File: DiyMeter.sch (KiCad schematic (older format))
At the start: 87 parts

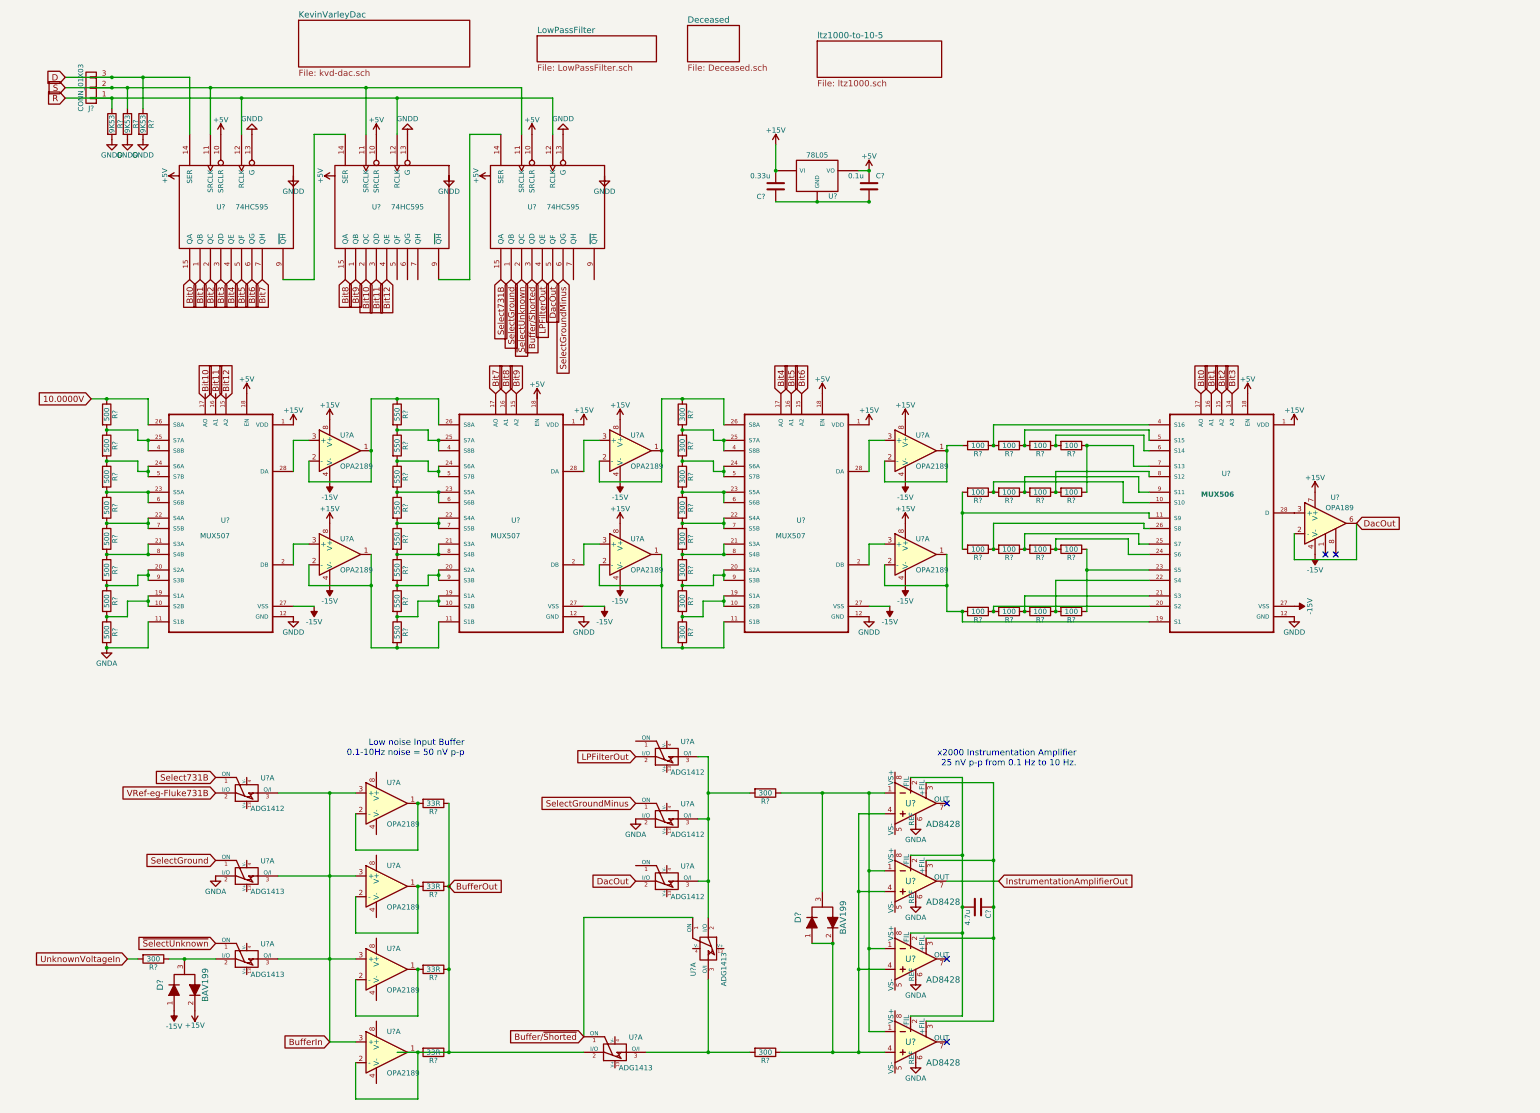
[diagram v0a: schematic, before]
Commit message: Add files via upload
Updated opamps to ada4522 because they have lower bias current.
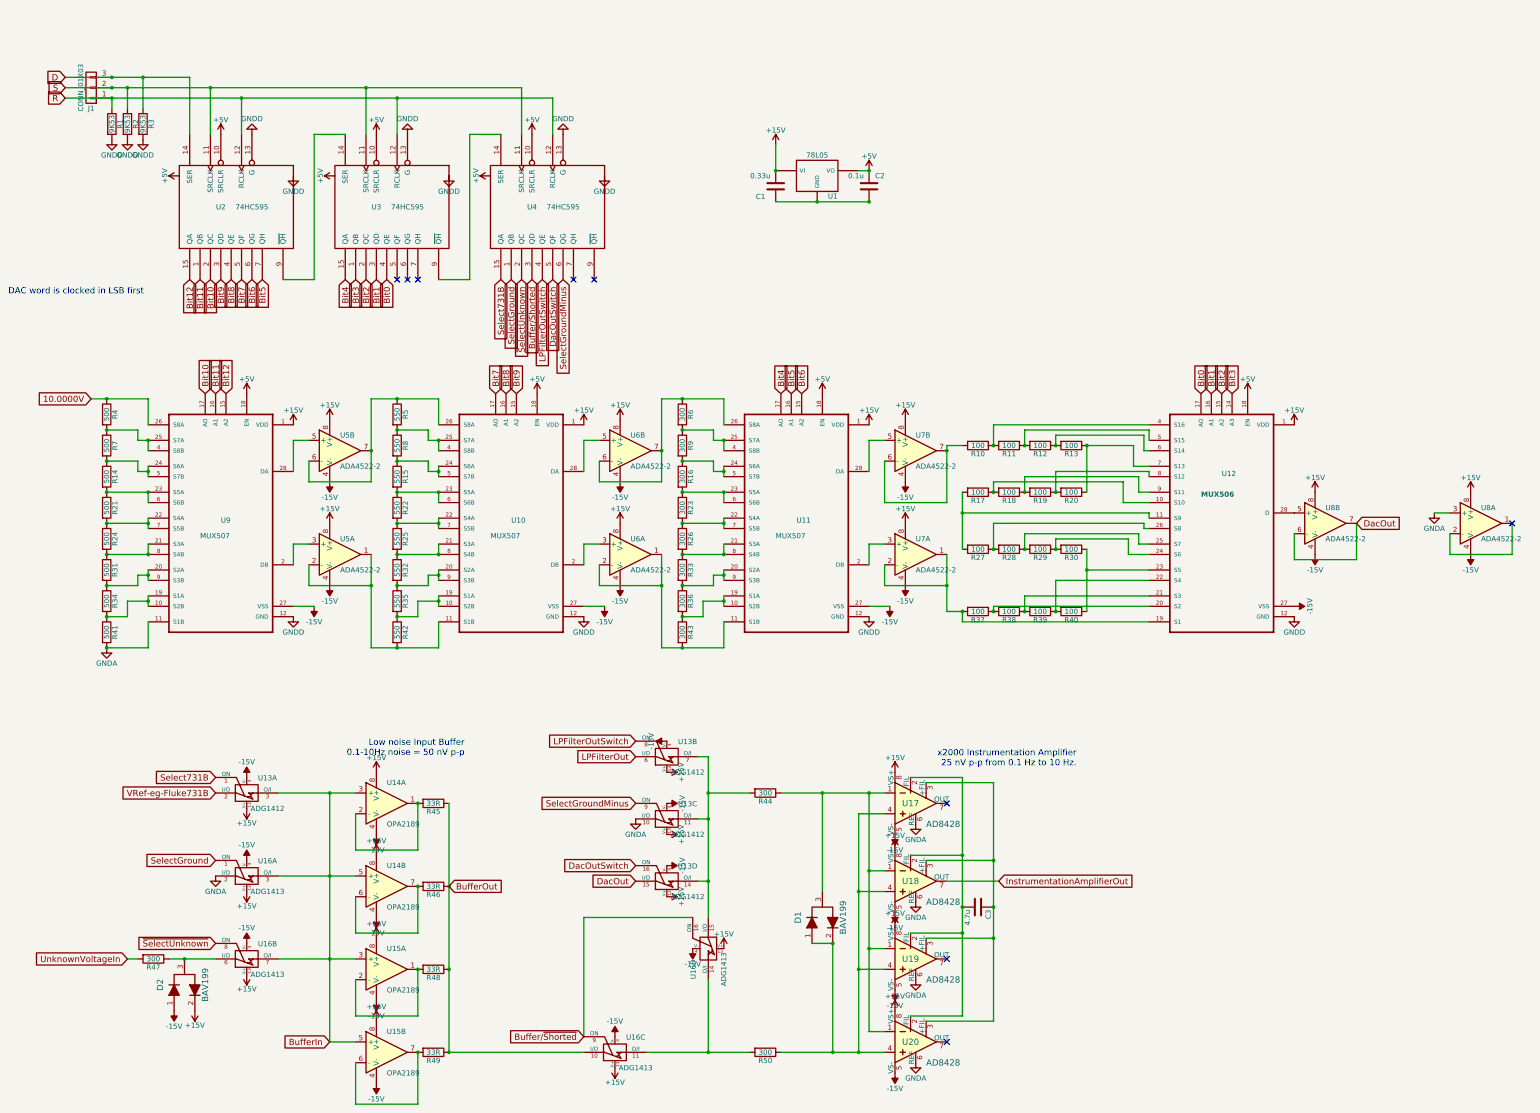
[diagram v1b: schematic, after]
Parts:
- removed U?: OPA189, symbol OP07
- added U8: ADA4522-2, symbol OP275
- U5, U6, U7: renamed from U?; value OPA2189 -> ADA4522-2
- gave numbers to parts that had none: 72
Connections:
- net +15V: now also U13.13 (V+), U13.13 (V+), U13.13 (V+), U13.13 (V+), U14.8 (V+), U14.8 (V+), U15.8 (V+), U15.8 (V+), U16.13 (V+), U16.13 (V+), U16.13 (V+), U16.13 (V+), U17.8 (VS+), U18.8 (VS+), U19.8 (VS+), U20.8 (VS+), U8.8 (V+), U8.8 (V+)
- net +5V: now also U10.18 (EN)
- net -15V: now also U13.4 (V-), U13.4 (V-), U13.4 (V-), U13.4 (V-), U14.4 (V-), U14.4 (V-), U15.4 (V-), U15.4 (V-), U16.4 (V-), U16.4 (V-), U16.4 (V-), U16.4 (V-), U17.5 (VS-), U18.5 (VS-), U19.5 (VS-), U20.5 (VS-), U8.4 (V-), U8.4 (V-)
- net Bit0: now also U3.4 (QE); no longer U2.15 (QA)
- net Bit1: now also U3.3 (QD); no longer U2.1 (QB)
- net Bit10: now also U2.2 (QC), U9.17 (AO); no longer U3.2 (QC)
- net Bit11: now also U2.1 (QB), U9.16 (A1); no longer U3.3 (QD)
- net Bit12: now also U2.15 (QA), U9.15 (A2); no longer U3.4 (QE)
- net Bit2: now also U3.2 (QC); no longer U2.2 (QC)
- net Bit3: now also U3.1 (QB); no longer U2.3 (QD)
- net Bit4: now also U3.15 (QA); no longer U2.4 (QE)
- net Bit5: now also U2.7 (QH); no longer U2.5 (QF)
- net Bit7: now also U2.5 (QF); no longer U2.7 (QH)
- net Bit8: now also U2.4 (QE); no longer U3.15 (QA)
- net Bit9: now also U2.3 (QD); no longer U3.1 (QB)
- net Buffer/~Shorted: now also U16.16 (ON), U16.9 (ON); no longer U16.1 (ON), U16.1 (ON)
- net BufferIn: now also U14.5 (+), U15.5 (+), U16.7 (O/I); no longer U14.3 (+), U15.3 (+), U16.3 (O/I)
- net BufferOut: now also U16.10 (I/O); no longer R49.2, U15.1, U15.2 (-), U16.2 (I/O)
- net DacOut: now also U13.15 (I/O), U8.6 (-), U8.7; no longer U13.2 (I/O), U4.5 (QF)
- net GNDA: now also U13.10 (I/O), U8.3 (+); no longer U13.2 (I/O)
- net LPFilterOut: now also U13.6 (I/O); no longer U13.2 (I/O), U4.4 (QE)
- net SelectGroundMinus: now also U13.9 (ON); no longer U13.1 (ON)
- net ~SelectUnknown: now also U16.8 (ON); no longer U16.1 (ON)
- net at U9.2 (DB): now also U5.3 (+); no longer U5.3 (+)
- net at U9.28 (DA): now also U5.5 (+); no longer U5.3 (+)
- net at R42.2, U10.11 (S1B): now also U5.1, U5.2 (-); no longer U5.1, U5.2 (-)
- net at R5.1, U10.26 (S8A): now also U5.6 (-), U5.7; no longer U5.1, U5.2 (-)
- net at U10.2 (DB): now also U6.3 (+); no longer U6.3 (+)
- net at U10.28 (DA): now also U6.5 (+); no longer U6.3 (+)
- net at R43.2, U11.11 (S1B): now also U6.1, U6.2 (-); no longer U6.1, U6.2 (-)
- net at R6.1, U11.26 (S8A): now also U6.6 (-), U6.7; no longer U6.1, U6.2 (-)
- net at U11.2 (DB): now also U7.3 (+); no longer U7.3 (+)
- net at U11.28 (DA): now also U7.5 (+); no longer U7.3 (+)
- net at R37.2, U12.19 (S1): now also U7.1, U7.2 (-); no longer U7.1, U7.2 (-)
- net at U12.28 (D): now also U8.5 (+)
- net at D2.3, R47.1: now also U16.6 (I/O); no longer U16.2 (I/O)
- new net: R10.2, U7.6 (-), U7.7
- new net: R44.2, U13.11 (O/I), U13.14 (O/I), U13.7 (O/I), U16.15 (I/O)
- new net: R50.2, U16.11 (O/I), U16.14 (O/I)
- new net: R46.2, U14.6 (-), U14.7
- new net: R49.2, U15.6 (-), U15.7
- new net: U8.1, U8.2 (-)
- new net DacOutSwitch: U13.16 (ON), U4.5 (QF)
- new net LPFilterOutSwitch: U13.8 (ON), U4.4 (QE)
- no-connect marks 5 -> 9
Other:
- note added: "DAC word is clocked in LSB first"
- moved on the sheet: U5A, U6A, U7A
